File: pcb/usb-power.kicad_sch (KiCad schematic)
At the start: 7 parts, among them J2 USB4110-GF-A, U9 AP2112K-3.3

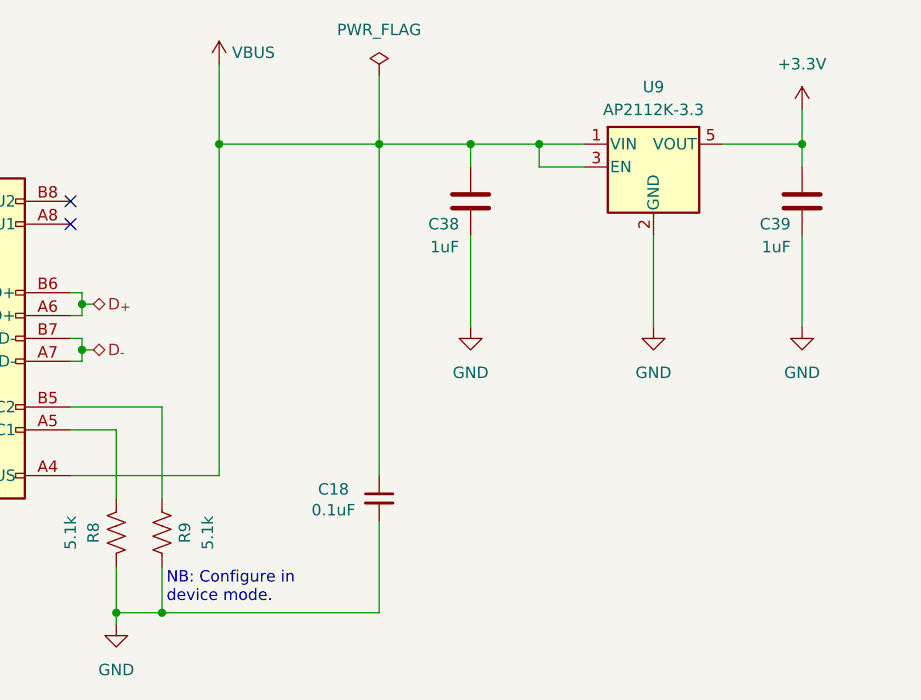
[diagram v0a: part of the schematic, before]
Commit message: Revision E
- Resolve issues 1-11
- Add pdf of rev d schematic for easy comparison
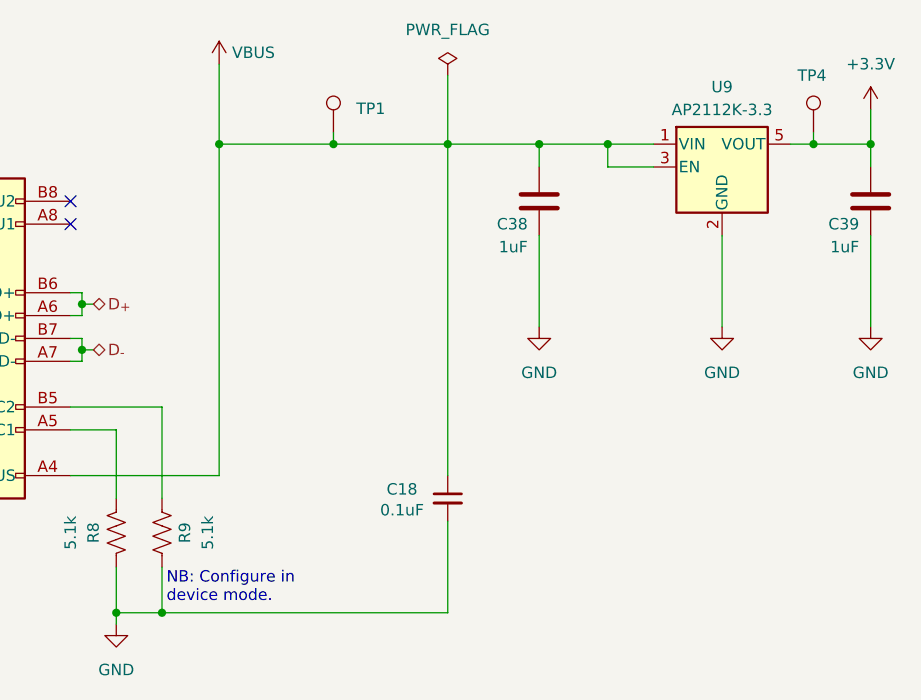
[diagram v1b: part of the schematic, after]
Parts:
- added TP1, TP4: ~, TestPoint:TestPoint_Pad_D2.0mm, symbol Connector:TestPoint
- C18: footprint Capacitor_SMD:C_0603_1608Metric -> Capacitor_SMD:C_0402_1005Metric
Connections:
- net +3.3V: now also TP4.1
- net VBUS: now also TP1.1
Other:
- moved on the sheet: C18, C38, C39, U9

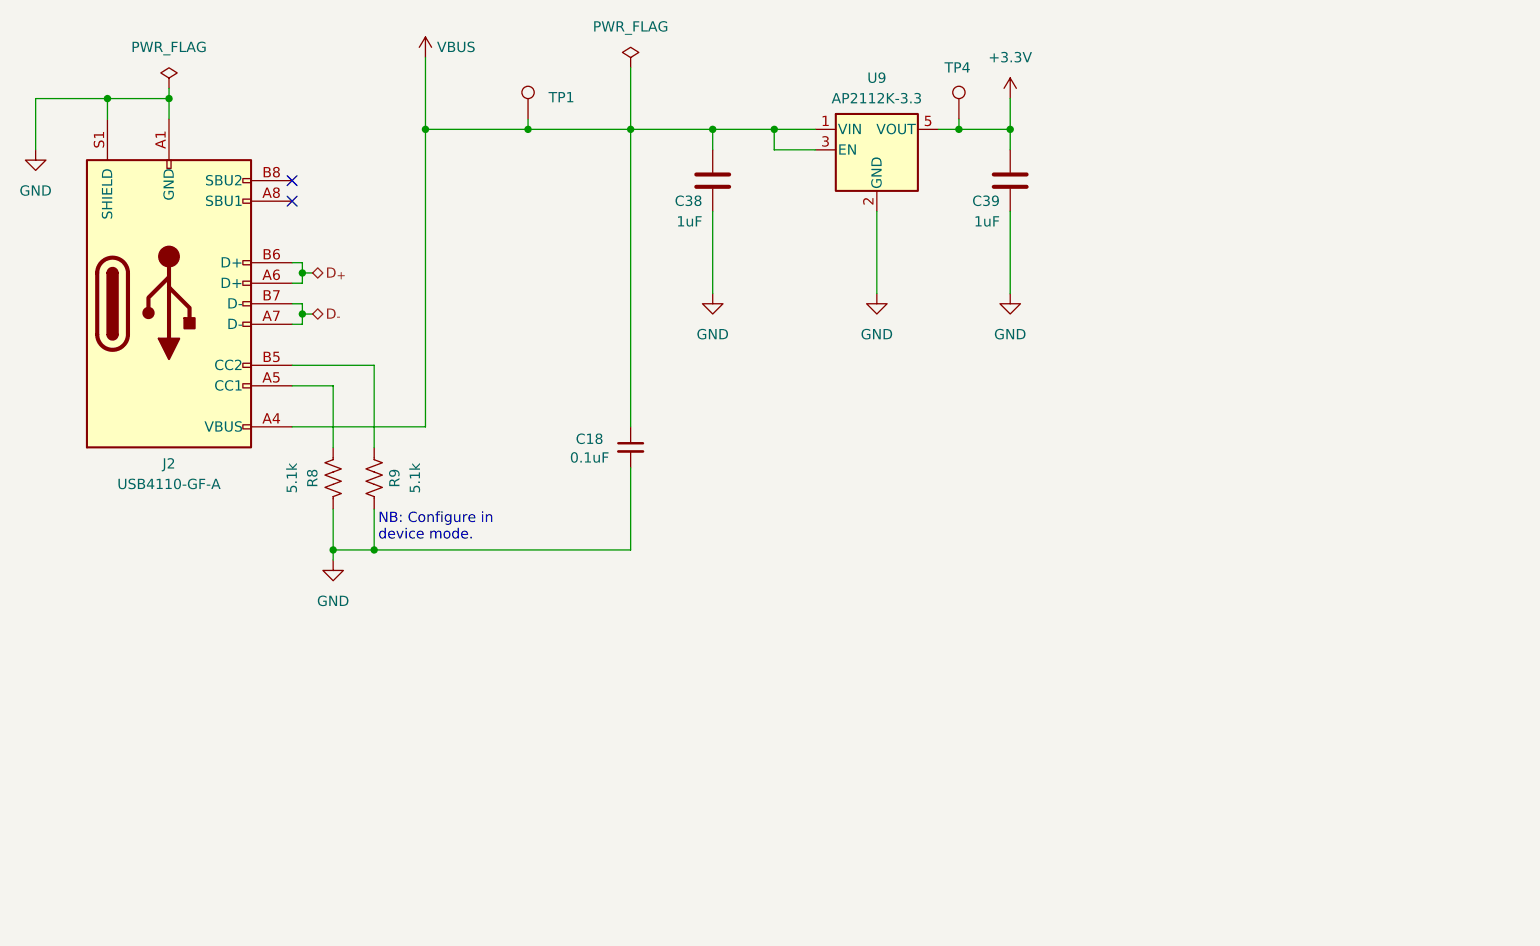
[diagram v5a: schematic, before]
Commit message: Final edits to rev G before fab
- Move USB connector twoards board edge by 1.5mm
- Make all silk text uniform
- Add required stackup and board characteristics to user.comments layer
- Redo 3.3V power routing to RP2040 (one power pin was not connected)
- Uniform schematic sheet size
- And many other small changes
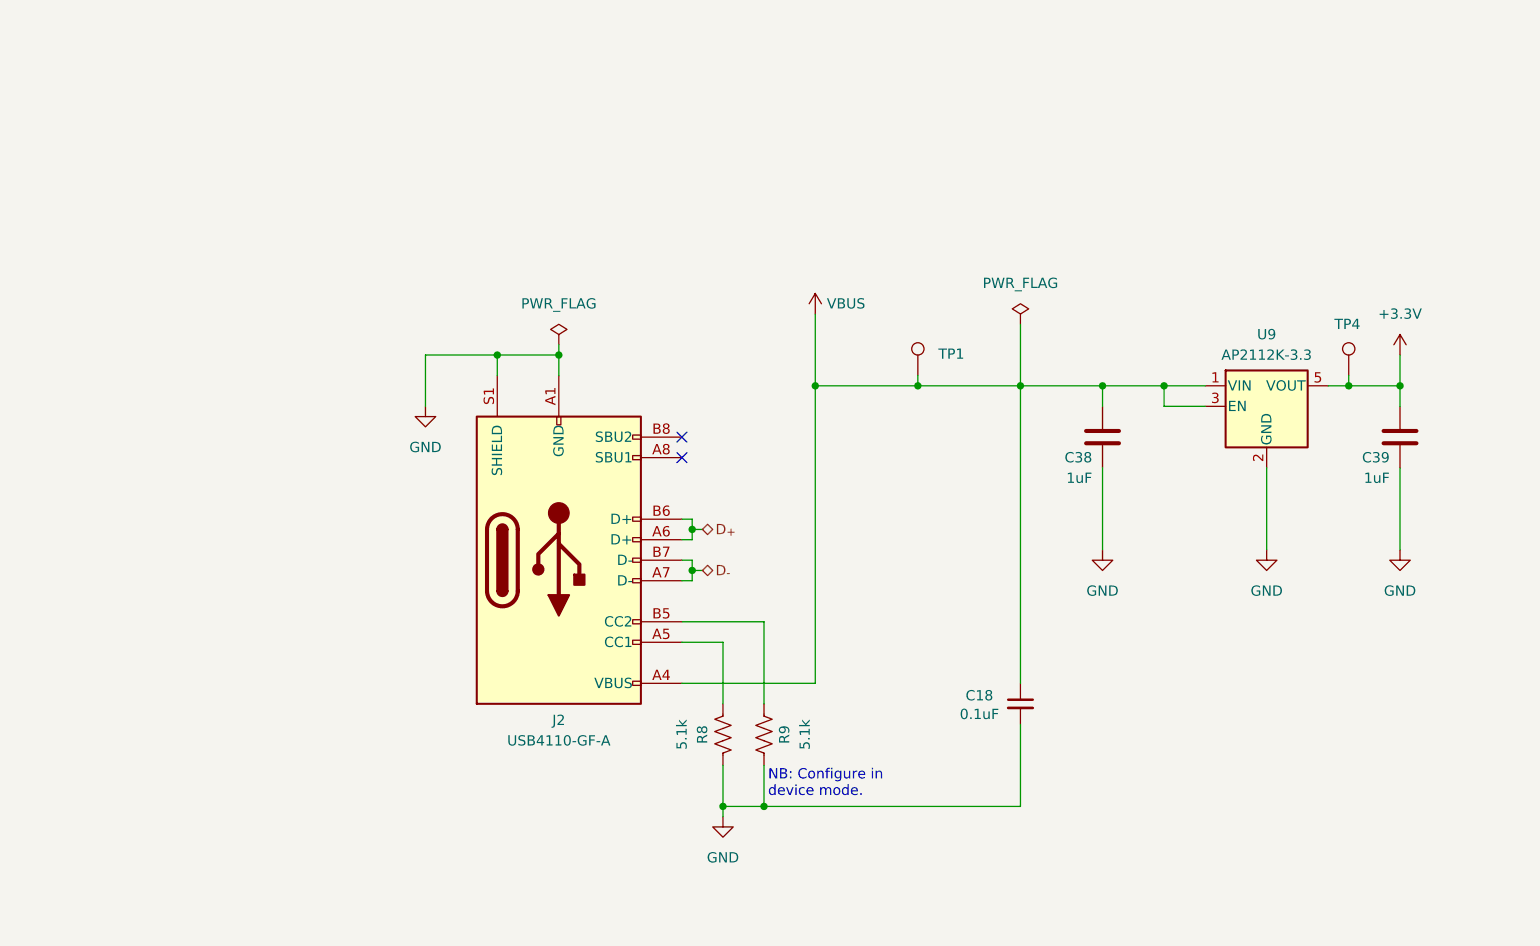
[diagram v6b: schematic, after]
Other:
- moved on the sheet: C18, C38, C39, J2, R8, R9, TP1, TP4, U9

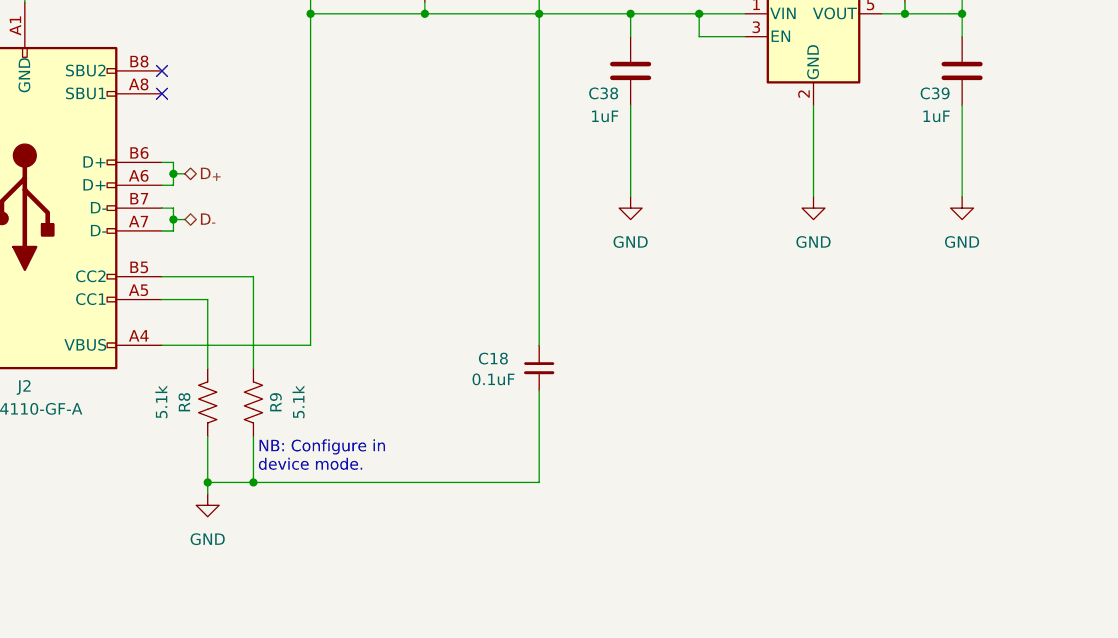
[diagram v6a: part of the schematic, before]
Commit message: Add USB diode protection
- Change revision g -> h
  - schematic
  - pcb
  - silk screen
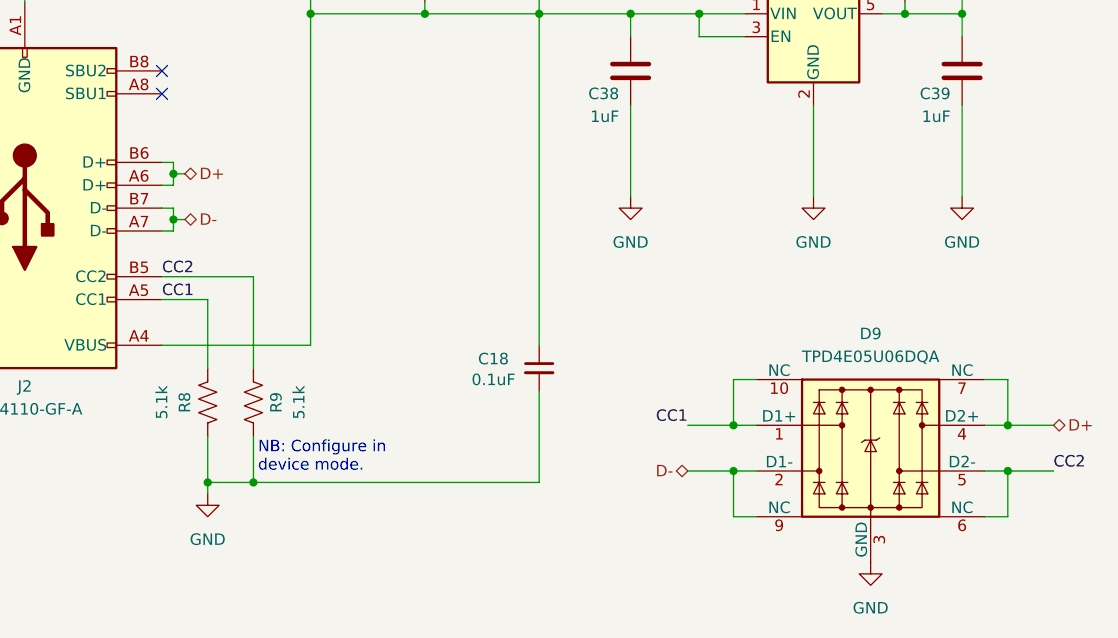
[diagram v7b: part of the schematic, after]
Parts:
- added D9: TPD4E05U06DQA, Package_SON:USON-10_2.5x1.0mm_P0.5mm, symbol Power_Protection:TPD4E05U06DQA
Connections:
- net GND: now also D9.3 (GND), D9.8 (GND)
- net CC2: now reaches J2.B5 (CC2), R9.2
- net CC2: now also D9.5 (D2-), D9.6 (NC)
- net CC1: now reaches J2.A5 (CC1), R8.2
- net CC1: now also D9.1 (D1+), D9.10 (NC)
- net D_{+} renamed D+
- net D+: now also D9.4 (D2+), D9.7 (NC)
- net D_{-} renamed D-
- net D-: now also D9.2 (D1-), D9.9 (NC)

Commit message: Add 3d parts
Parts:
- J2: footprint Connector_USB:USB_C_Receptacle_GCT_USB4110 -> open-ephys:USB_C_Receptacle_GCT_USB4110
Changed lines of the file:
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@@
 			)
 		)
-		(property "Footprint" "Connector_USB:USB_C_Receptacle_GCT_USB4110"
+		(property "Footprint" "open-ephys:USB_C_Receptacle_GCT_USB4110"
 			(at 109.22 95.25 0)
 			(effects
